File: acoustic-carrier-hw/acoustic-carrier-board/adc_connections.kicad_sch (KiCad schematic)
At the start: 27 parts, among them IC1 ECP5-BGA256, J2 Conn_02x08_Odd_Even, U7 MS9280

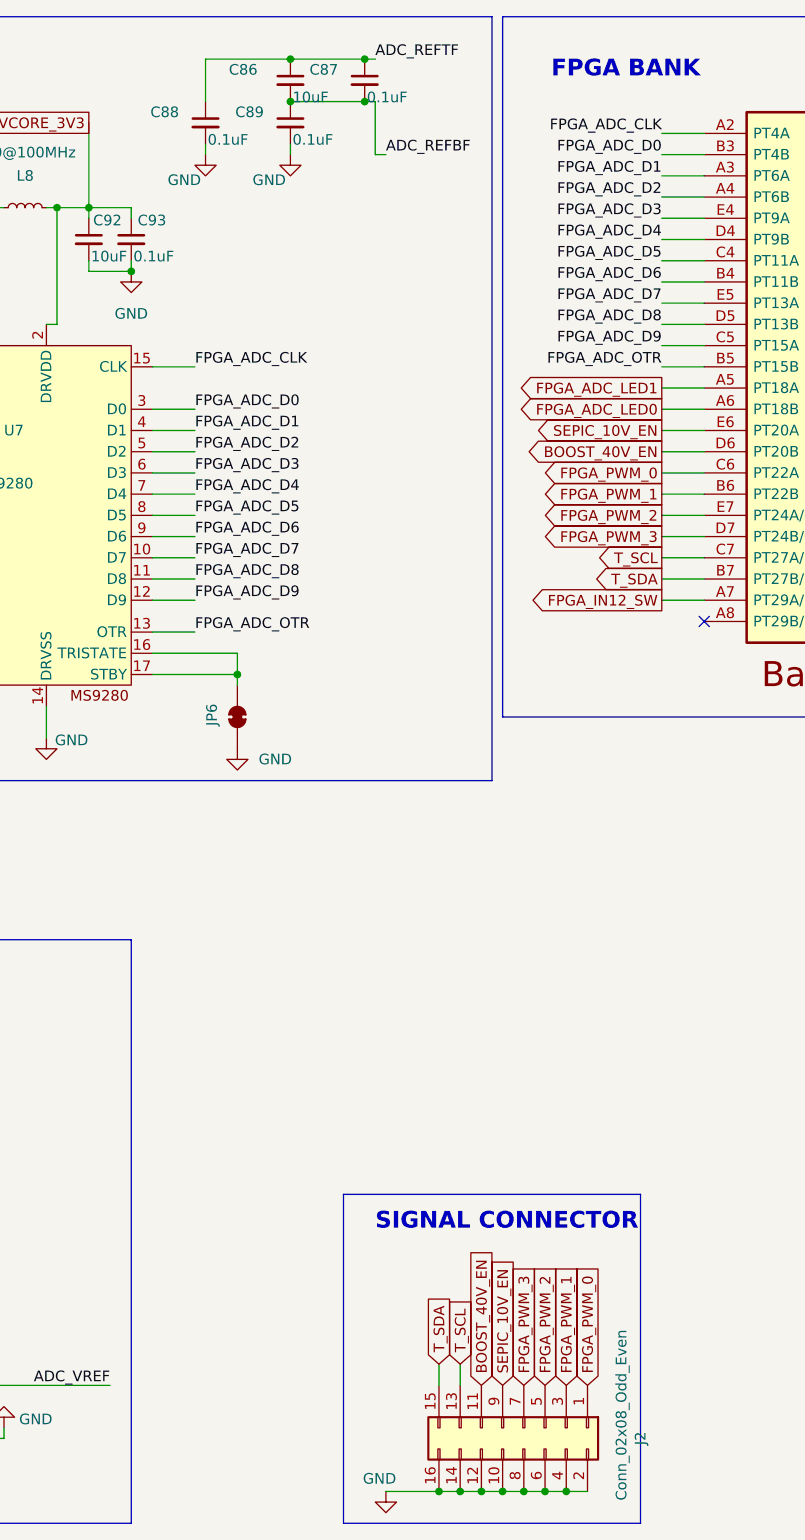
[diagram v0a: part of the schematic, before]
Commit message: [carrier] Fixed minor symbol errors, added minor routing info (next) continue schematic check
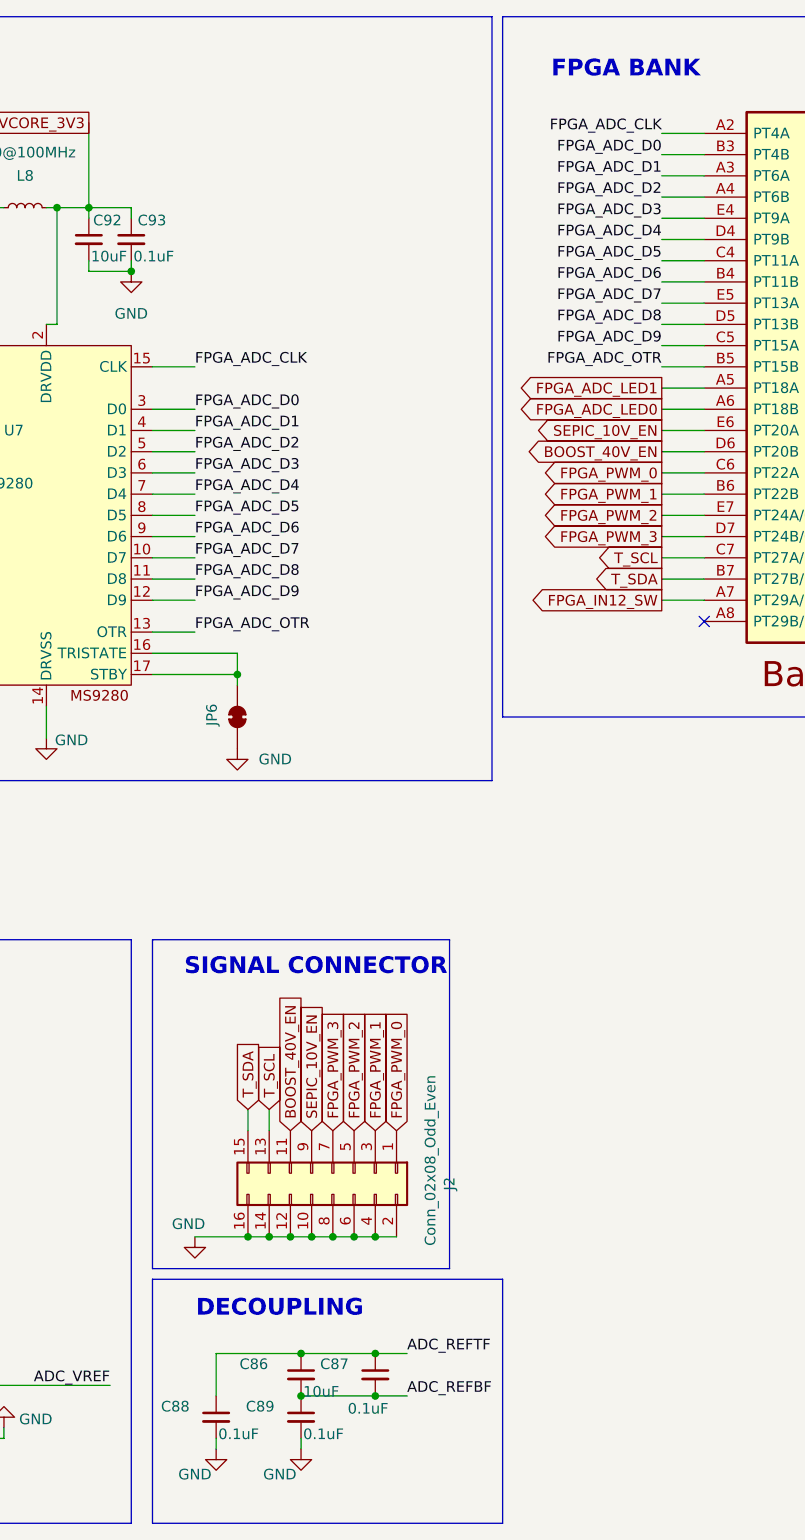
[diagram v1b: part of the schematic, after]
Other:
- note added: "DECOUPLING"
- moved on the sheet: C86, C87, C88, C89, J2

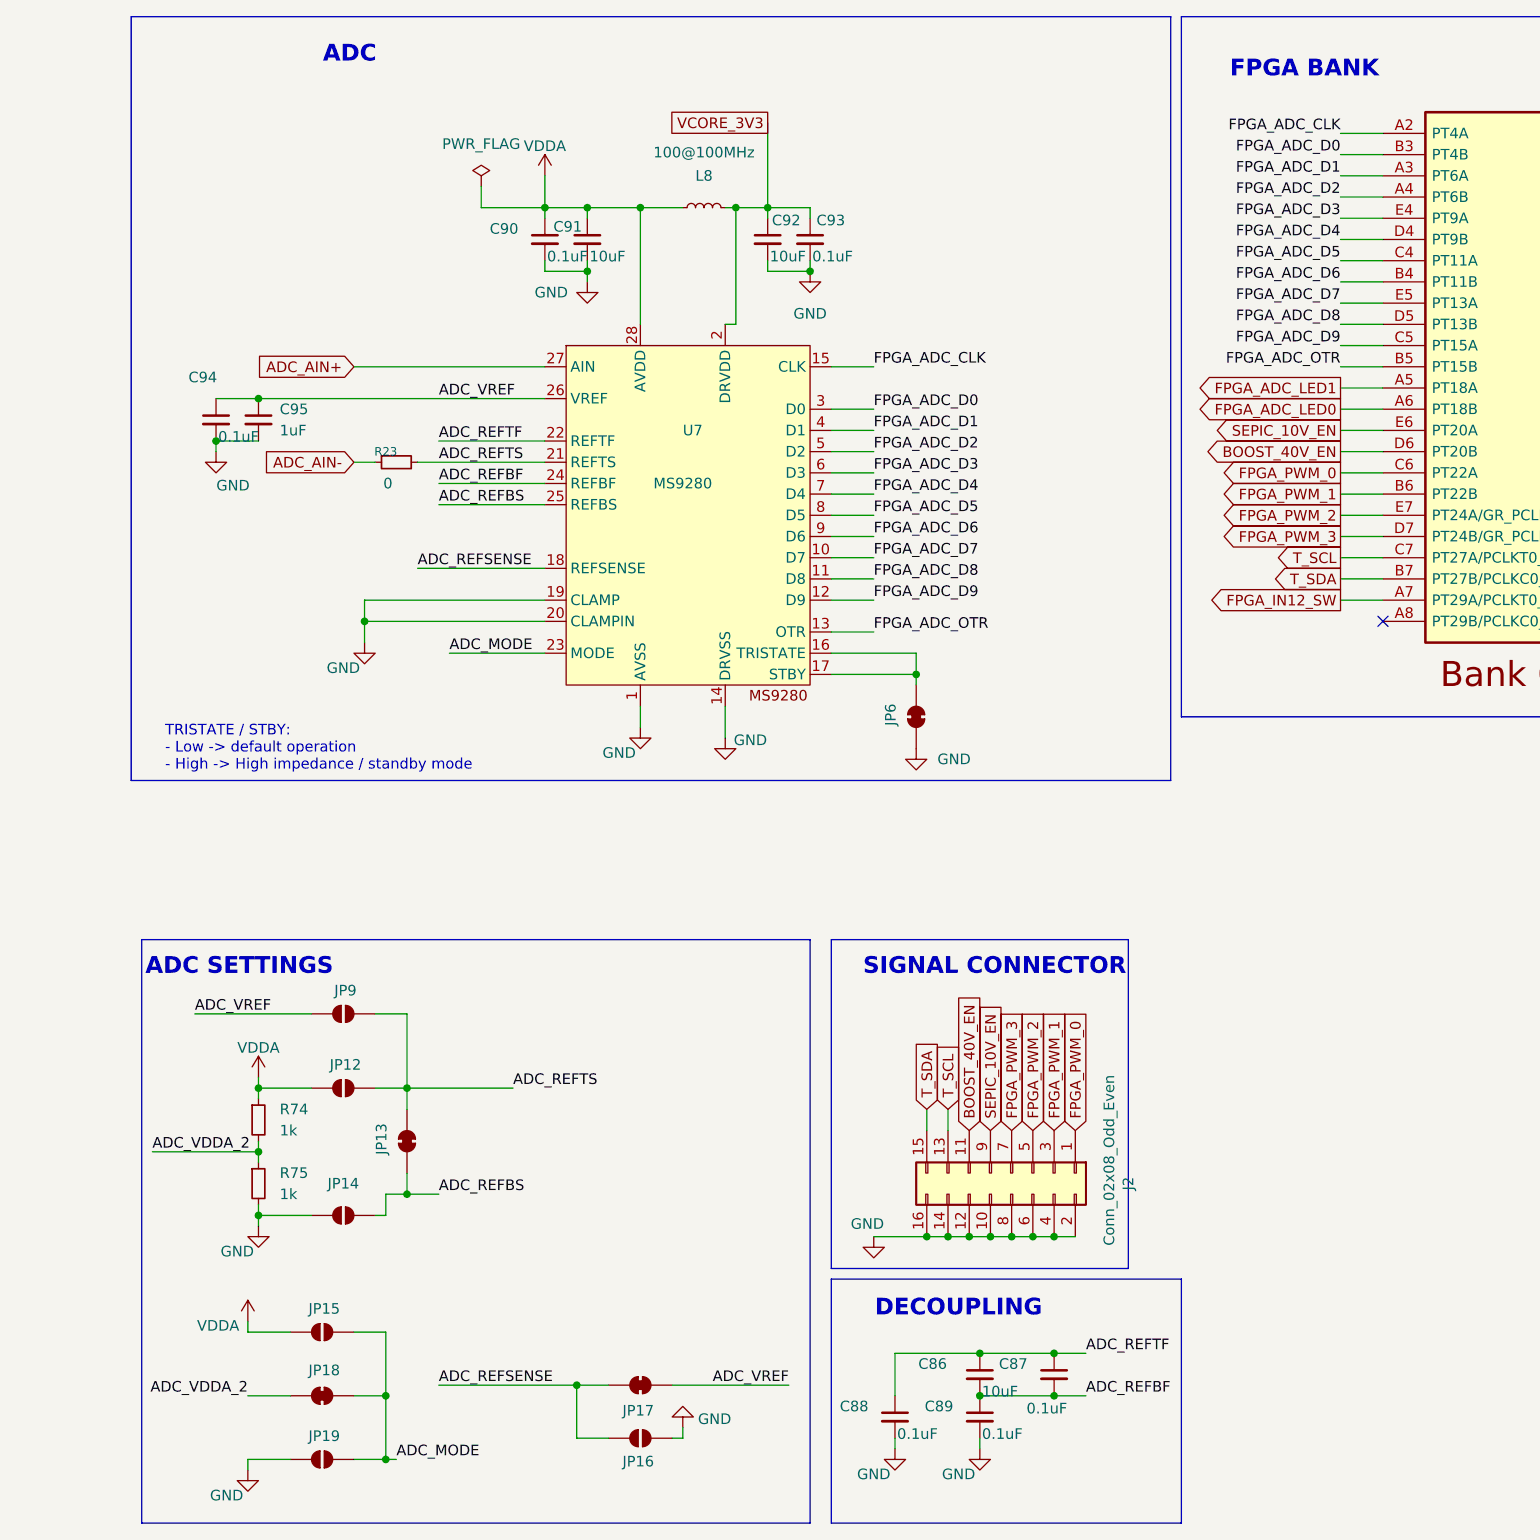
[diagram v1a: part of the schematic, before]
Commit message: [carrier] Review of adc_connections-page done
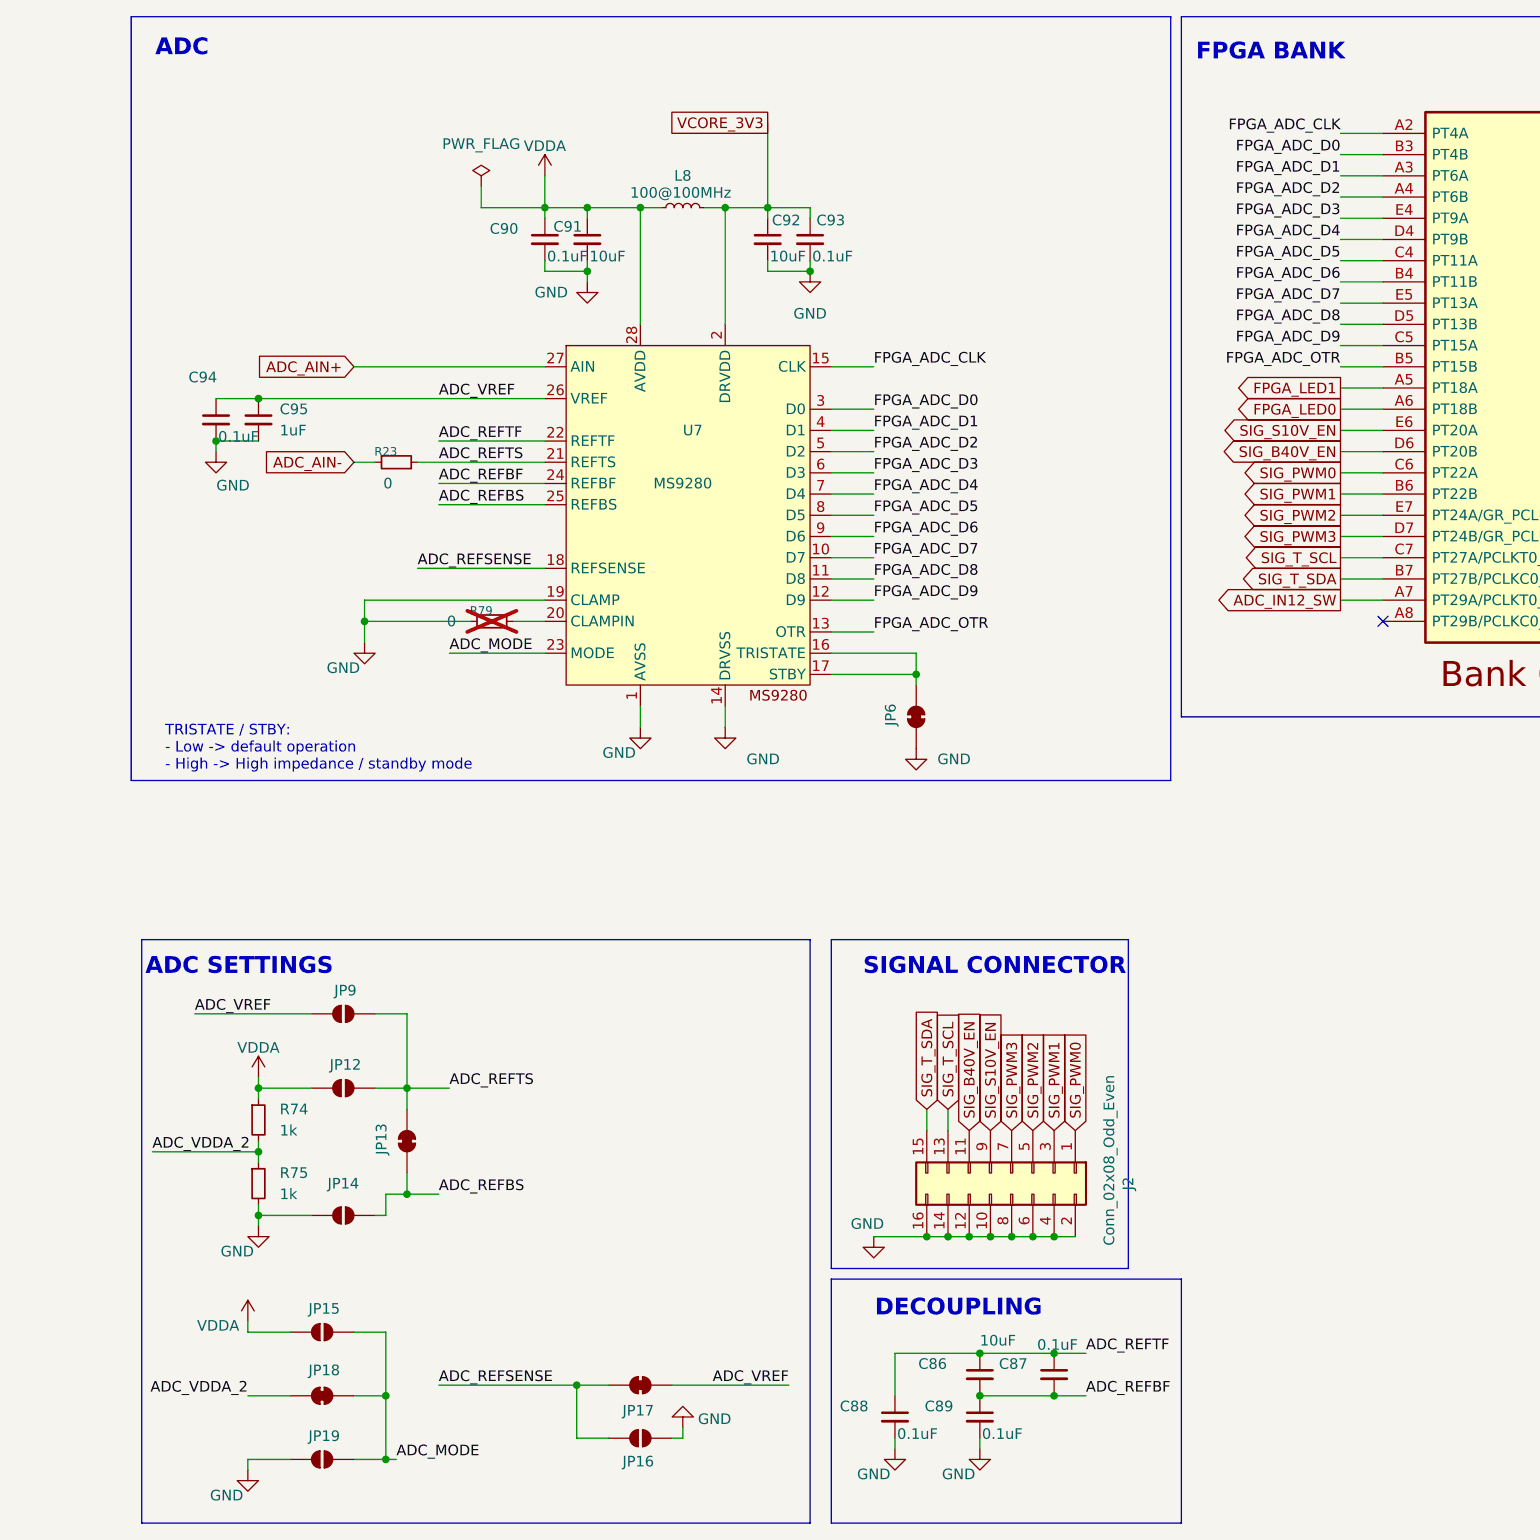
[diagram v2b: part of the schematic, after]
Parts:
- added R79: 0, Resistor_SMD:R_0603_1608Metric, symbol Device:R_Small
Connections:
- net GND: now also R79.1; no longer U7.20 (CLAMPIN)
- net BOOST_40V_EN renamed SIG_B40V_EN
- net FPGA_ADC_LED0 renamed FPGA_LED0
- net FPGA_ADC_LED1 renamed FPGA_LED1
- net FPGA_IN12_SW renamed ADC_IN12_SW
- net FPGA_PWM_0 renamed SIG_PWM0
- net FPGA_PWM_1 renamed SIG_PWM1
- net FPGA_PWM_2 renamed SIG_PWM2
- net FPGA_PWM_3 renamed SIG_PWM3
- net SEPIC_10V_EN renamed SIG_S10V_EN
- net T_SCL renamed SIG_T_SCL
- net T_SDA renamed SIG_T_SDA
- new net: R79.2, U7.20 (CLAMPIN)
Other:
- moved on the sheet: L8

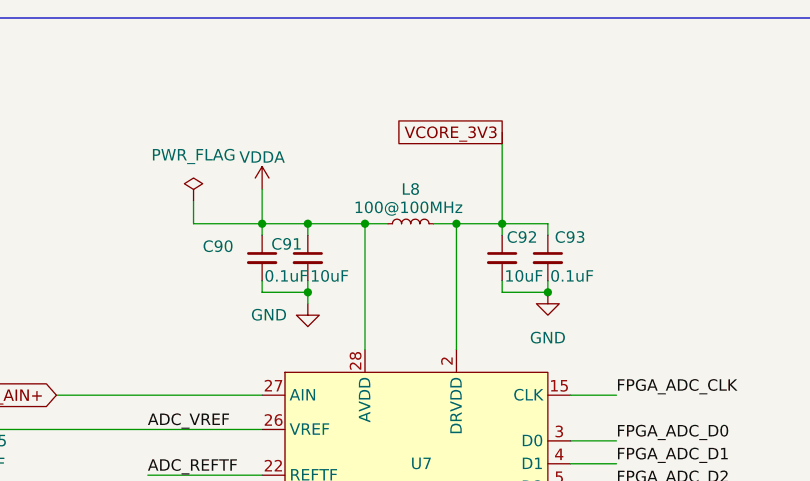
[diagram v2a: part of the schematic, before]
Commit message: [carrier] Added separate buses for ddr3 ctrl-cmd and dq-groups
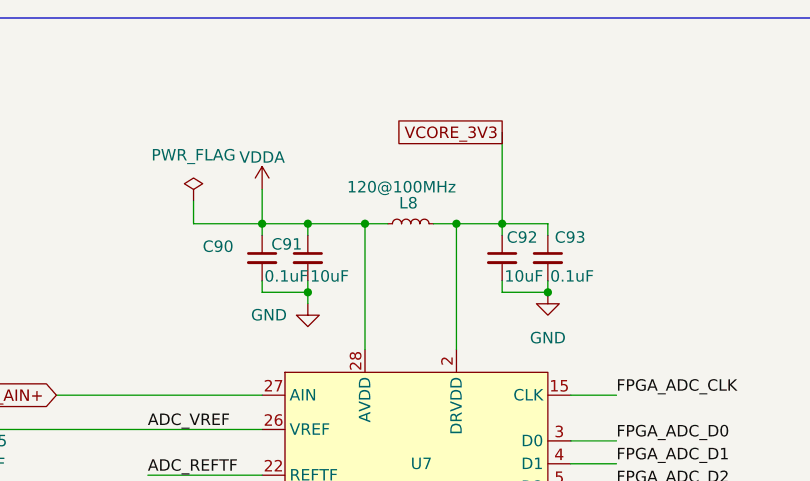
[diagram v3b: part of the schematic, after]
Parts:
- L8: value 100@100MHz -> 120@100MHz; footprint Inductor_SMD:L_0805_2012Metric -> Inductor_SMD:L_0603_1608Metric; LPN C1015 -> C113030; MPN GZ2012D101TF -> BLM18SG121TN1D
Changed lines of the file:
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@@
-	)
-	(symbol
-		(lib_id "Device:L_Small")
-		(at 80.01 38.1 270)
-		(mirror x)
-		(unit 1)
-		(exclude_from_sim no)
-		(in_bom yes)
-		(on_board yes)
-		(dnp no)
-		(property "Reference" "L8"
-			(at 80.01 34.29 90)
-			(effects
-				(font
-					(size 1.27 1.27)
-				)
-			)
-		)
-		(property "Value" "100@100MHz"
-			(at 79.756 36.322 90)
-			(effects
-				(font
-					(size 1.27 1.27)
-				)
-			)
-		)
-		(property "Footprint" "Inductor_SMD:L_0805_2012Metric"
-			(at 80.01 38.1 0)
-			(effects
-				(font
-					(size 1.27 1.27)
-				)
-				(hide yes)
-			)
-		)
-		(property "Datasheet" "https://evelta.com/content/datasheets/212-Ferrite-2012.pdf?srsltid=AfmBOooIaIBTDyAN72yrZoxwkUca105kmrozh_WidW95l5Oggr1J46Nq"
-			(at 80.01 38.1 0)
-			(effects
-				(font
-					(size 1.27 1.27)
-				)
-				(hide yes)
-			)
-		)
-		(property "Description" "Inductor, small symbol"
-			(at 80.01 38.1 0)
-			(effects
-				(font
-					(size 1.27 1.27)
-				)
-				(hide yes)
-			)
-		)
-		(property "LPN" "C1015"
-			(at 80.01 38.1 90)
-			(effects
-				(font
-					(size 1.27 1.27)
-				)
-				(hide yes)
-			)
-		)
-		(property "MPN" "GZ2012D101TF"
-			(at 80.01 38.1 90)
-			(effects
-				(font
-					(size 1.27 1.27)
-				)
-				(hide yes)
-			)
-		)
-		(pin "1"
-		)
-		(pin "2"
-		)
-		(instances
-			(project "acoustic-carrier-board"
-				(path "/25b015c9-ab13-4427-b72c-b6f348597100/94142f45-8b3d-48ce-ac4d-b9c7695832d7"
-					(reference "L8")
-					(unit 1)
-				)
-			)
-		)
 	)
 	(symbol
@@
 					(unit 1)
 				)
+			)
+		)
+	)
+	(symbol
+		(lib_id "Device:L_Small")
+		(at 80.01 38.1 270)
+		(mirror x)
+		(unit 1)
+		(exclude_from_sim no)
+		(in_bom yes)
+		(on_board yes)
+		(dnp no)
+		(property "Reference" "L8"
+			(at 79.756 35.814 90)
+			(effects
+				(font
+					(size 1.27 1.27)
+				)
+			)
+		)
+		(property "Value" "120@100MHz"
+			(at 78.994 34.036 90)
+			(effects
+				(font
+					(size 1.27 1.27)
+				)
+			)
+		)
+		(property "Footprint" "Inductor_SMD:L_0603_1608Metric"
+			(at 80.01 38.1 0)
+			(effects
+				(font
+					(size 1.27 1.27)
+				)
+				(hide yes)
+			)
+		)
+		(property "Datasheet" "https://jlcpcb.com/api/file/downloadByFileSystemAccessId/8588898925176217600"
+			(at 80.01 38.1 0)
+			(effects
+				(font
+					(size 1.27 1.27)
+				)
+				(hide yes)
+			)
+		)
+		(property "Description" "25mOhm, 1-3A"
+			(at 80.01 38.1 0)
+			(effects
+				(font
+					(size 1.27 1.27)
+				)
+				(hide yes)
+			)
+		)
+		(property "LPN" "C113030"
+			(at 80.01 38.1 90)
+			(effects
+				(font
+					(size 1.27 1.27)
+				)
+				(hide yes)
+			)
+		)
+		(property "MPN" "BLM18SG121TN1D"
+			(at 80.01 38.1 90)
+			(effects
+				(font
+					(size 1.27 1.27)
+				)
+				(hide yes)
+			)
+		)
+		(property "Part Number" ""
+			(at 80.01 38.1 90)
+			(effects
+				(font
+					(size 1.27 1.27)
+				)
+				(hide yes)
+			)
+		)
+		(property "SN-DK" ""
+			(at 80.01 38.1 90)
+			(effects
+				(font
+					(size 1.27 1.27)
+				)
+				(hide yes)
+			)
+		)
+		(property "Sim.Pin" ""
+			(at 80.01 38.1 90)
+			(effects
+				(font
+					(size 1.27 1.27)
+				)
+				(hide yes)
+			)
+		)
+		(property "LCSC Part" ""
+			(at 80.01 38.1 90)
+			(effects
+				(font
+					(size 1.27 1.27)
+				)
+				(hide yes)
+			)
+		)
+		(pin "1"
+		)
+		(pin "2"
+		)
+		(instances
+			(project "acoustic-carrier-board"
+				(path "/25b015c9-ab13-4427-b72c-b6f348597100/94142f45-8b3d-48ce-ac4d-b9c7695832d7"
+					(reference "L8")
+					(unit 1)
+				)
